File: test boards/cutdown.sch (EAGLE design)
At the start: 12 parts, among them Q1 FDD3706, U1 6N138M

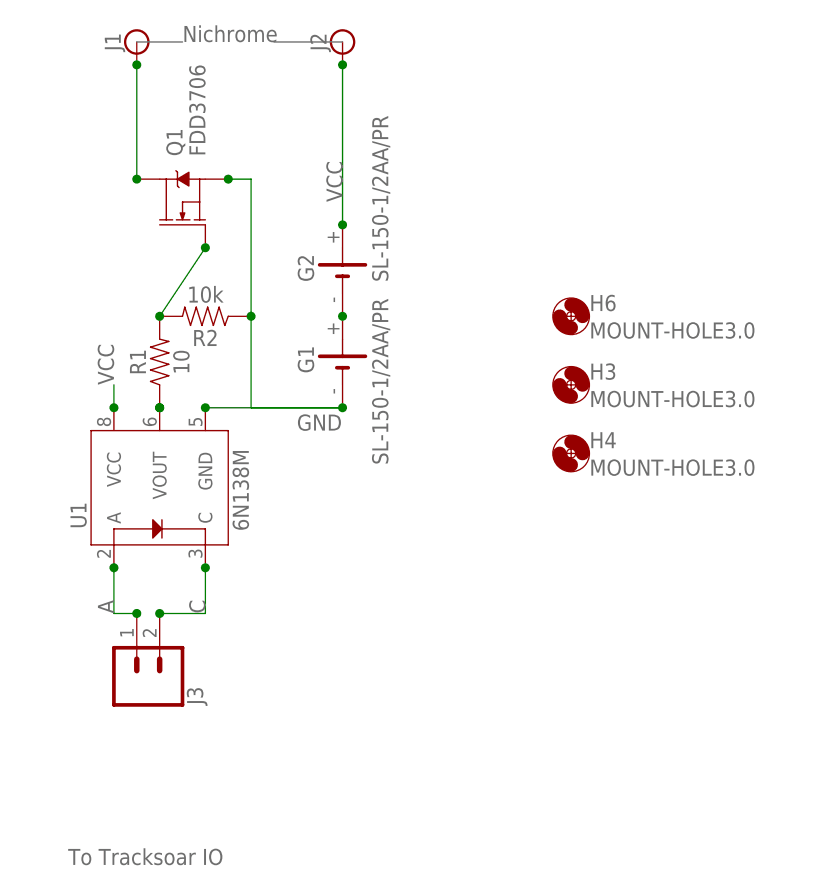
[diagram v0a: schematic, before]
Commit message: Added boards
Added boards for a cutdown circuit, spi flash storage and spi flash breakout board and a shield template.
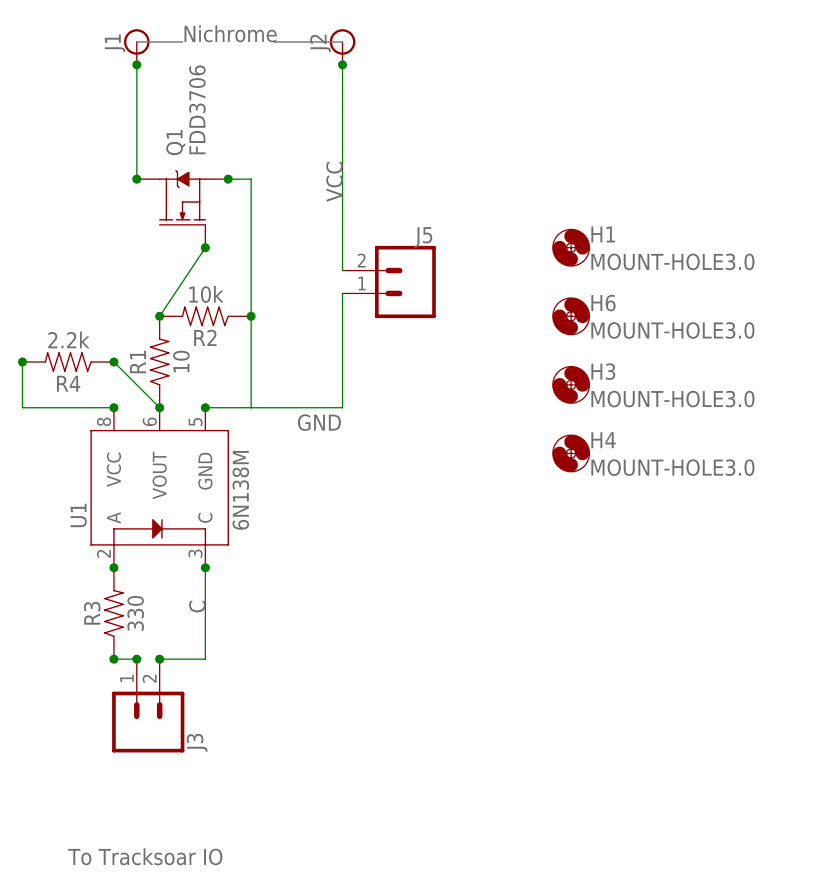
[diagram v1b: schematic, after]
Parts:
- removed G1, G2: SL-150-1/2AA/PR, battery:SL-150-1/2AA/PR
- added H1: MOUNT-HOLE3.0, holes:MOUNT-HOLE3.0
- added J5: (no value), SparkFun-Connectors:CONN_02PTH3
- added R3: 330, SparkFun-Resistors:10OHM-0603-1/10W-1%
- added R4: 2.2k, SparkFun-Resistors:10OHM-0603-1/10W-1%
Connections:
- removed net N$1: G1.+, G2.-
- new net N$5: R3.2, U1.A
- new net N$6: R4.2, U1.VCC
- net A: now also R3.1; no longer U1.A
- net GND: now also J5.1; no longer G1.-
- net N$4: now also R4.1
- net VCC: now also J5.2; no longer G2.+, U1.VCC
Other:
- moved on the sheet: J3
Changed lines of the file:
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@@
 <parts>
 <part name="Q1" library="SparkFun-DiscreteSemi" library_urn="urn:adsk.eagle:library:514" deviceset="MOSFET-NCH" device="-FDD8780" package3d_urn="urn:adsk.eagle:package:38459/1" value="FDD3706"/>
-<part name="G1" library="battery" library_urn="urn:adsk.eagle:library:109" deviceset="SL-150-1/2AA/PR" device="" package3d_urn="urn:adsk.eagle:package:4607/1"/>
-<part name="G2" library="battery" library_urn="urn:adsk.eagle:library:109" deviceset="SL-150-1/2AA/PR" device="" package3d_urn="urn:adsk.eagle:package:4607/1"/>
 <part name="H3" library="holes" library_urn="urn:adsk.eagle:library:237" deviceset="MOUNT-HOLE" device="3.0" package3d_urn="urn:adsk.eagle:package:14277/1"/>
 <part name="H4" library="holes" library_urn="urn:adsk.eagle:library:237" deviceset="MOUNT-HOLE" device="3.0" package3d_urn="urn:adsk.eagle:package:14277/1"/>
@@
 <part name="R1" library="SparkFun-Resistors" library_urn="urn:adsk.eagle:library:532" deviceset="10OHM" device="-0603-1/10W-1%" package3d_urn="urn:adsk.eagle:package:39650/1" value="10"/>
 <part name="R2" library="SparkFun-Resistors" library_urn="urn:adsk.eagle:library:532" deviceset="10KOHM" device="-0603-1/10W-1%" package3d_urn="urn:adsk.eagle:package:39650/1" value="10k"/>
+<part name="R3" library="SparkFun-Resistors" library_urn="urn:adsk.eagle:library:532" deviceset="10OHM" device="-0603-1/10W-1%" package3d_urn="urn:adsk.eagle:package:39650/1" value="330"/>
+<part name="R4" library="SparkFun-Resistors" library_urn="urn:adsk.eagle:library:532" deviceset="10OHM" device="-0603-1/10W-1%" package3d_urn="urn:adsk.eagle:package:39650/1" value="2.2k"/>
+<part name="H1" library="holes" library_urn="urn:adsk.eagle:library:237" deviceset="MOUNT-HOLE" device="3.0" package3d_urn="urn:adsk.eagle:package:14277/1"/>
+<part name="J5" library="SparkFun-Connectors" library_urn="urn:adsk.eagle:library:513" deviceset="CONN_02" device="PTH3" package3d_urn="urn:adsk.eagle:package:38048/1"/>
 </parts>
 <sheets>
@@
 <instances>
 <instance part="Q1" gate="NMOS" x="50.8" y="96.52" rot="R90"/>
-<instance part="G1" gate="G$1" x="68.58" y="78.74" smashed="yes" rot="R90">
-<attribute name="NAME" x="65.405" y="77.47" size="1.778" layer="95" rot="R90"/>
-<attribute name="VALUE" x="73.66" y="67.31" size="1.778" layer="96" rot="R90"/>
-</instance>
-<instance part="G2" gate="G$1" x="68.58" y="88.9" rot="R90"/>
 <instance part="H3" gate="G$1" x="93.98" y="76.2"/>
 <instance part="H4" gate="G$1" x="93.98" y="68.58"/>
@@
 <instance part="J1" gate="G$1" x="45.72" y="114.3" rot="R90"/>
 <instance part="J2" gate="G$1" x="68.58" y="114.3" rot="R90"/>
-<instance part="J3" gate="G$1" x="45.72" y="43.18" rot="MR90"/>
+<instance part="J3" gate="G$1" x="45.72" y="38.1" rot="MR90"/>
 <instance part="R1" gate="G$1" x="48.26" y="78.74" rot="R90"/>
 <instance part="R2" gate="G$1" x="53.34" y="83.82" rot="R180"/>
+<instance part="R3" gate="G$1" x="43.18" y="50.8" rot="R90"/>
+<instance part="R4" gate="G$1" x="38.1" y="78.74" rot="R180"/>
+<instance part="H1" gate="G$1" x="93.98" y="91.44"/>
+<instance part="J5" gate="G$1" x="76.2" y="86.36" rot="MR0"/>
 </instances>
 <busses>
@@
 <pinref part="U1" gate="G$1" pin="GND"/>
 <label x="63.5" y="71.12" size="1.778" layer="95"/>
-<pinref part="G1" gate="G$1" pin="-"/>
-<junction x="68.58" y="73.66"/>
-<wire x1="53.34" y1="73.66" x2="68.58" y2="73.66" width="0.1524" layer="91"/>
+<wire x1="53.34" y1="73.66" x2="58.42" y2="73.66" width="0.1524" layer="91"/>
 <pinref part="Q1" gate="NMOS" pin="S"/>
 <wire x1="55.88" y1="99.06" x2="58.42" y2="99.06" width="0.1524" layer="91"/>
@@
 <junction x="58.42" y="83.82"/>
 <junction x="53.34" y="73.66"/>
+<wire x1="68.58" y1="86.36" x2="68.58" y2="73.66" width="0.1524" layer="91"/>
+<pinref part="J5" gate="G$1" pin="1"/>
 </segment>
 </net>
 <net name="VCC" class="0">
-<segment>
-<pinref part="U1" gate="G$1" pin="VCC"/>
-<wire x1="43.18" y1="73.66" x2="43.18" y2="76.2" width="0.1524" layer="91"/>
-<junction x="43.18" y="73.66"/>
-<label x="43.18" y="76.2" size="1.778" layer="95" rot="R90"/>
-</segment>
 <segment>
 <pinref part="J2" gate="G$1" pin="1"/>
@@
 </segment>
 <segment>
-<pinref part="G2" gate="G$1" pin="+"/>
-<wire x1="68.58" y1="93.98" x2="68.58" y2="106.68" width="0.1524" layer="91"/>
-<junction x="68.58" y="93.98"/>
+<wire x1="68.58" y1="88.9" x2="68.58" y2="106.68" width="0.1524" layer="91"/>
 <label x="68.58" y="96.52" size="1.778" layer="95" rot="R90"/>
+<pinref part="J5" gate="G$1" pin="2"/>
 </segment>
 </net>
 <net name="A" class="0">
 <segment>
-<pinref part="U1" gate="G$1" pin="A"/>
-<junction x="43.18" y="55.88"/>
-<label x="43.18" y="50.8" size="1.778" layer="95" rot="R90"/>
 <pinref part="J3" gate="G$1" pin="1"/>
-<wire x1="45.72" y1="50.8" x2="43.18" y2="50.8" width="0.1524" layer="91"/>
-<junction x="45.72" y="50.8"/>
-<wire x1="43.18" y1="55.88" x2="43.18" y2="50.8" width="0.1524" layer="91"/>
+<wire x1="45.72" y1="45.72" x2="43.18" y2="45.72" width="0.1524" layer="91"/>
+<junction x="45.72" y="45.72"/>
+<pinref part="R3" gate="G$1" pin="1"/>
+<junction x="43.18" y="45.72"/>
 </segment>
 </net>
@@
 <label x="53.34" y="50.8" size="1.778" layer="95" rot="R90"/>
 <pinref part="J3" gate="G$1" pin="2"/>
-<junction x="48.26" y="50.8"/>
-<wire x1="53.34" y1="55.88" x2="53.34" y2="50.8" width="0.1524" layer="91"/>
-<wire x1="53.34" y1="50.8" x2="48.26" y2="50.8" width="0.1524" layer="91"/>
-</segment>
-</net>
-<net name="N$1" class="0">
-<segment>
-<pinref part="G1" gate="G$1" pin="+"/>
-<pinref part="G2" gate="G$1" pin="-"/>
-<junction x="68.58" y="83.82"/>
+<junction x="48.26" y="45.72"/>
+<wire x1="53.34" y1="55.88" x2="53.34" y2="45.72" width="0.1524" layer="91"/>
+<wire x1="53.34" y1="45.72" x2="48.26" y2="45.72" width="0.1524" layer="91"/>
 </segment>
 </net>
@@
 <pinref part="U1" gate="G$1" pin="VOUT"/>
 <pinref part="R1" gate="G$1" pin="1"/>
+<pinref part="R4" gate="G$1" pin="1"/>
+<wire x1="43.18" y1="78.74" x2="48.26" y2="73.66" width="0.1524" layer="91"/>
 <junction x="48.26" y="73.66"/>
-<junction x="48.26" y="73.66"/>
+<junction x="43.18" y="78.74"/>
 </segment>
 </net>
+<net name="N$5" class="0">
+<segment>
+<pinref part="U1" gate="G$1" pin="A"/>
+<pinref part="R3" gate="G$1" pin="2"/>
+<junction x="43.18" y="55.88"/>
+</segment>
+</net>
+<net name="N$6" class="0">
+<segment>
+<pinref part="U1" gate="G$1" pin="VCC"/>
+<pinref part="R4" gate="G$1" pin="2"/>
+<wire x1="43.18" y1="73.66" x2="33.02" y2="73.66" width="0.1524" layer="91"/>
+<wire x1="33.02" y1="73.66" x2="33.02" y2="78.74" width="0.1524" layer="91"/>
+<junction x="43.18" y="73.66"/>
+<junction x="33.02" y="78.74"/>
+</segment>
+</net>
